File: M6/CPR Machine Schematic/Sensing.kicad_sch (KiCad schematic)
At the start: 9 parts, among them J12 I2C Port, J8 Force Sensor, U3 MCP6004, U5 MCP3021A0T-E_OT

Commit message: Final PCB
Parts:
- R16: value 80.6 Ohm -> 80.6 kOhm
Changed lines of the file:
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@@
 	(rectangle
 		(start 19.685 27.94)
-		(end 128.905 102.87)
+		(end 128.27 97.155)
 		(stroke
 			(width 0)
@@
 			)
 		)
-		(property "Value" "80.6 Ohm"
+		(property "Value" "80.6 kOhm"
 			(at 58.42 66.04 90)
 			(effects

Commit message: Board V2 Final
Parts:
- C13, C_OPT1, J8, R16, R17: now left out of the parts list
- U3, U5: Notes (none) -> Have: 1
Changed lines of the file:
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@@
 		(unit 1)
 		(exclude_from_sim no)
-		(in_bom yes)
+		(in_bom no)
 		(on_board yes)
 		(dnp yes)
@@
 		)
 		(property "digikey" "1292-1206N470J102CT-ND"
+			(at 74.93 54.61 0)
+			(effects
+				(font
+					(size 1.27 1.27)
+				)
+				(hide yes)
+			)
+		)
+		(property "Notes" ""
 			(at 74.93 54.61 0)
 			(effects
@@
 			)
 		)
+		(property "Notes" ""
+			(at 35.56 21.59 0)
+			(effects
+				(font
+					(size 1.27 1.27)
+				)
+				(hide yes)
+			)
+		)
 		(pin "2"
 		)
@@
 			)
 		)
+		(property "Notes" "Have: 1"
+			(at 102.87 48.26 0)
+			(effects
+				(font
+					(size 1.27 1.27)
+				)
+				(hide yes)
+			)
+		)
 		(pin "3"
 		)
@@
 		(unit 1)
 		(exclude_from_sim no)
-		(in_bom yes)
+		(in_bom no)
 		(on_board yes)
 		(dnp no)
@@
 			)
 		)
+		(property "Notes" ""
+			(at 40.64 86.36 0)
+			(effects
+				(font
+					(size 1.27 1.27)
+				)
+				(hide yes)
+			)
+		)
 		(pin "2"
 		)
@@
 		(unit 1)
 		(exclude_from_sim no)
-		(in_bom yes)
+		(in_bom no)
 		(on_board yes)
 		(dnp no)
@@
 			)
 		)
+		(property "Notes" ""
+			(at 58.42 80.01 90)
+			(effects
+				(font
+					(size 1.27 1.27)
+				)
+				(hide yes)
+			)
+		)
 		(pin "1"
 		)
@@
 		(unit 1)
 		(exclude_from_sim no)
-		(in_bom yes)
+		(in_bom no)
 		(on_board yes)
 		(dnp no)
@@
 			)
 		)
+		(property "Notes" ""
+			(at 58.42 69.85 90)
+			(effects
+				(font
+					(size 1.27 1.27)
+				)
+				(hide yes)
+			)
+		)
 		(pin "2"
 		)
@@
 			)
 		)
+		(property "Notes" "Have: 1"
+			(at 59.69 48.26 0)
+			(effects
+				(font
+					(size 1.27 1.27)
+				)
+				(hide yes)
+			)
+		)
 		(pin "4"
 		)
@@
 			)
 		)
+		(property "Notes" ""
+			(at 34.29 49.53 0)
+			(effects
+				(font
+					(size 1.27 1.27)
+				)
+				(hide yes)
+			)
+		)
 		(pin "2"
 		)
@@
 		(unit 1)
 		(exclude_from_sim no)
-		(in_bom yes)
+		(in_bom no)
 		(on_board yes)
 		(dnp no)
@@
 			(at 34.29 41.91 0)
 			(effects
+				(font
+					(size 1.27 1.27)
+				)
+				(hide yes)
+			)
+		)
+		(property "Notes" ""
+			(at 34.29 41.91 0)
+			(effects

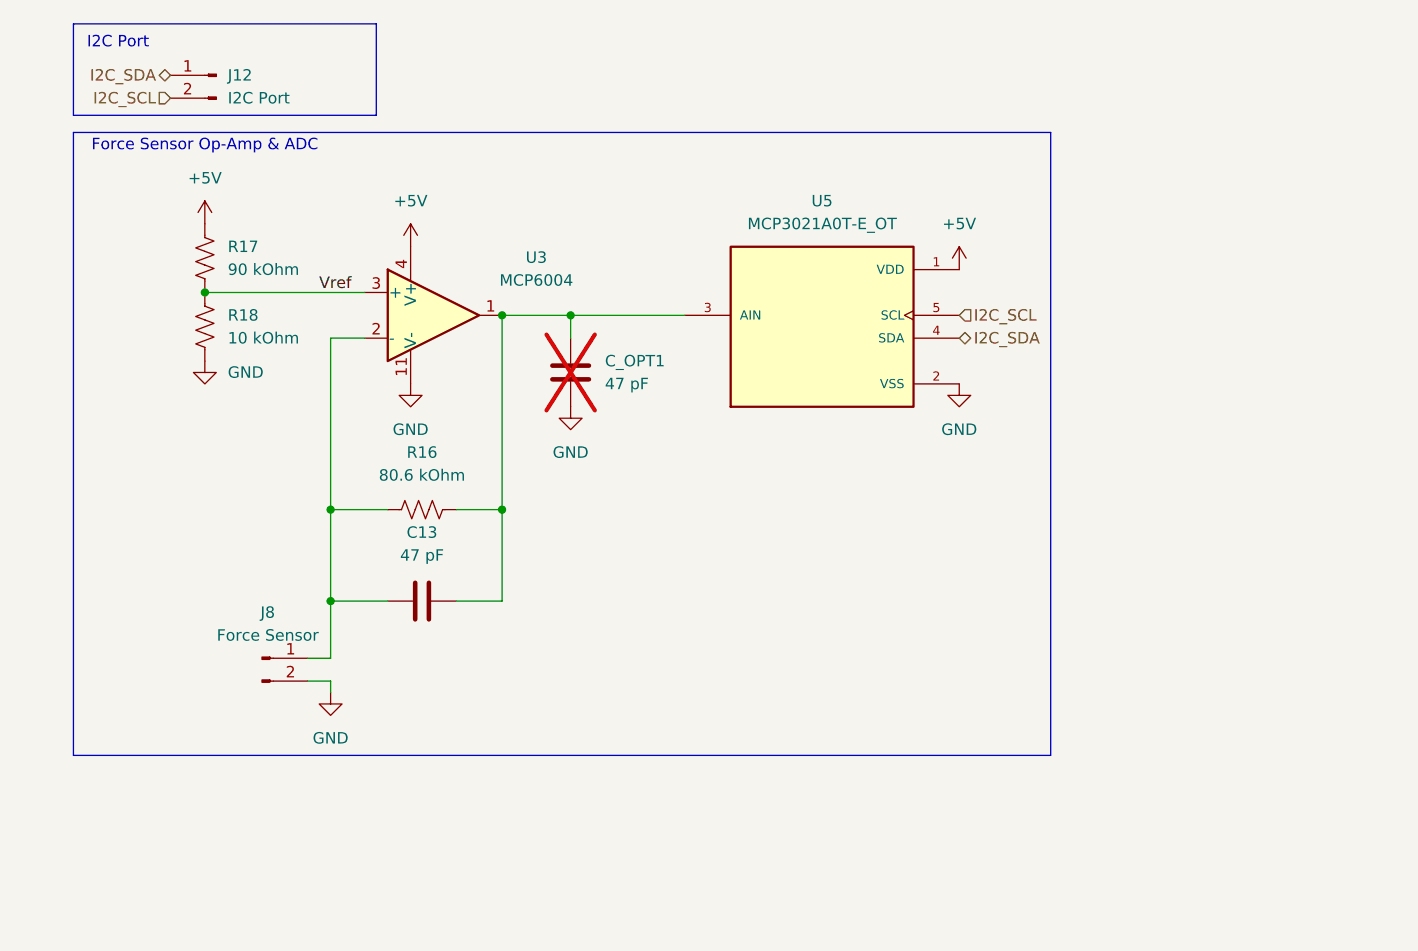
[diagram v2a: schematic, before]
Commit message: Voltage readout, MUX, Debouncing Caps
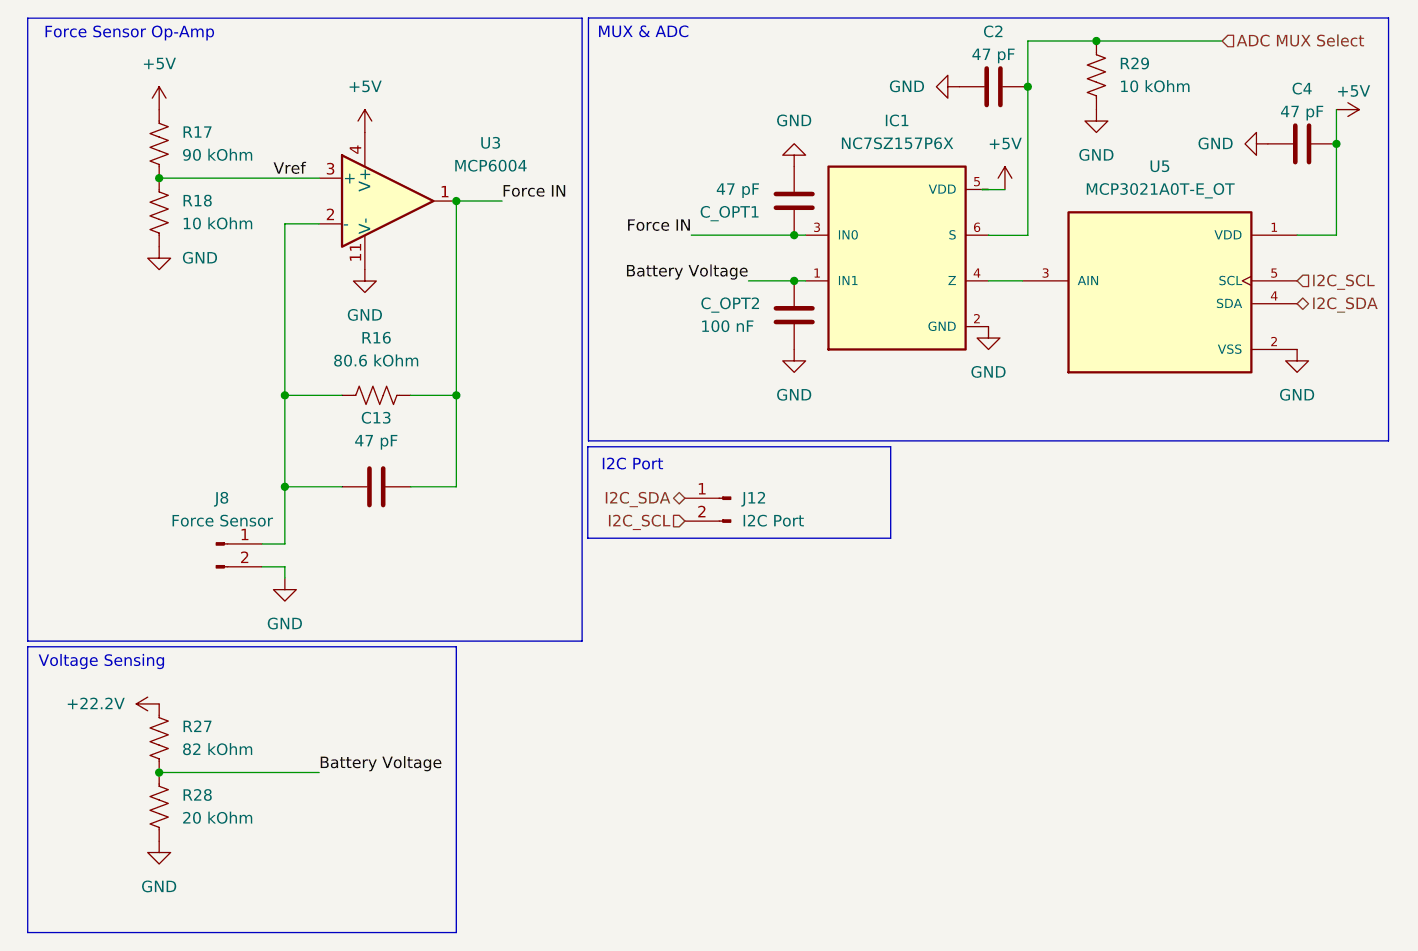
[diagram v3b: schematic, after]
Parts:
- added C2, C4: 47 pF, Capacitor_SMD:C_1206_3216Metric_Pad1.33x1.80mm_HandSolder, symbol Device:C
- added C_OPT2: 100 nF, Capacitor_SMD:C_1206_3216Metric_Pad1.33x1.80mm_HandSolder, symbol Device:C
- added IC1: NC7SZ157P6X, NC7SZ157P6X:SC70-6L, symbol NC7SZ157P6X:NC7SZ157P6X
- added R27: 82 kOhm, symbol Device:R_US
- added R28: 20 kOhm, symbol Device:R_US
- added R29: 10 kOhm, Resistor_SMD:R_1206_3216Metric_Pad1.30x1.75mm_HandSolder, symbol Device:R_US
- C_OPT1: now fitted; now in the parts list
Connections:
- net +5V: now also C4.2, IC1.5 (VDD)
- net GND: now also C2.1, C4.1, C_OPT2.1, IC1.2 (GND), R28.2, R29.2
- net Force IN: now reaches C13.2, C_OPT1.2, R16.1, U3.1
- net Force IN: now also IC1.3 (IN0); no longer U5.3 (AIN)
- new net: IC1.4 (Z), U5.3 (AIN)
- new net +22.2V: R27.1
- new net ADC MUX Select: C2.2, IC1.6 (S), R29.1
- new net Battery Voltage: C_OPT2.2, IC1.1 (IN1), R27.2, R28.1
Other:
- note added: "Force Sensor Op-Amp"
- note added: "MUX & ADC"
- note added: "Voltage Sensing"
- note removed: "Force Sensor Op-Amp & ADC"
- moved on the sheet: C13, J12, J8, R16, R17, R18, U3, U5

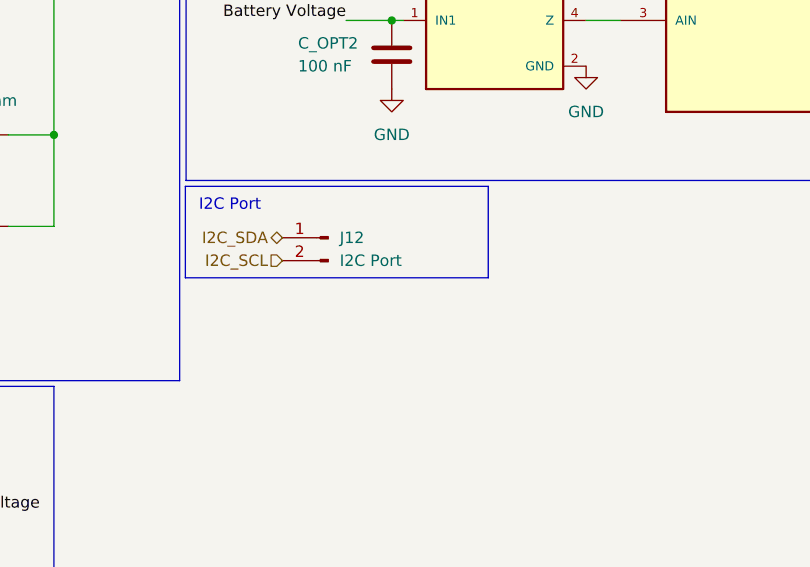
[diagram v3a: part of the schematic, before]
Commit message: MUX, Debounce Caps, I2C Testpoints
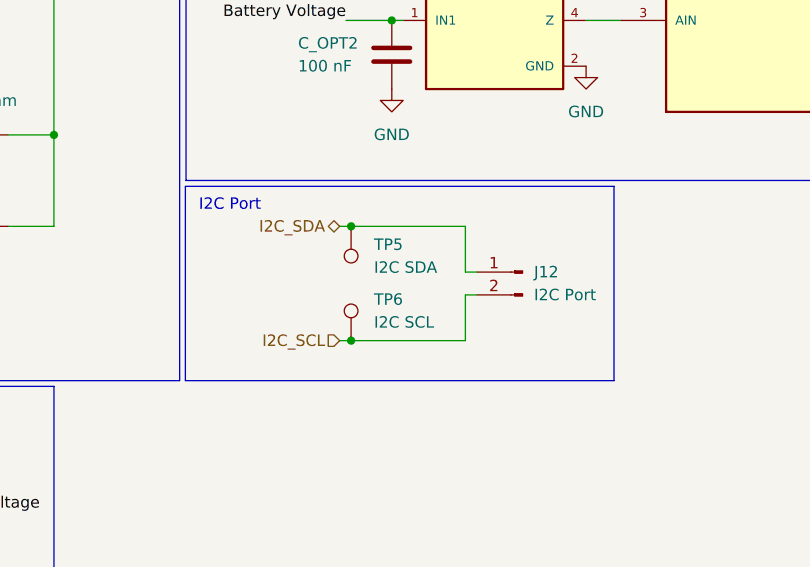
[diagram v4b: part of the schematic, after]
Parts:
- added TP5: I2C SDA, TestPoint:TestPoint_Pad_D3.0mm, symbol Connector:TestPoint
- added TP6: I2C SCL, TestPoint:TestPoint_Pad_D3.0mm, symbol Connector:TestPoint
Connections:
- net I2C_SCL: now also TP6.1
- net I2C_SDA: now also TP5.1
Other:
- moved on the sheet: J12
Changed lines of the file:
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@@
 	(rectangle
 		(start 76.835 62.865)
-		(end 110.49 73.025)
+		(end 124.46 84.455)
 		(stroke
 			(width 0)
@@
 	)
 	(junction
+		(at 95.25 67.31)
+		(diameter 0)
+		(color 0 0 0 0)
+	)
+	(junction
 		(at 43.18 67.31)
 		(diameter 0)
@@
 		(color 0 0 0 0)
 	)
+	(junction
+		(at 95.25 80.01)
+		(diameter 0)
+		(color 0 0 0 0)
+	)
 	(wire
 		(pts
@@
 	(wire
 		(pts
+			(xy 95.25 80.01) (xy 93.98 80.01)
+		)
+		(stroke
+			(width 0)
+			(type default)
+		)
+	)
+	(wire
+		(pts
 			(xy 99.7691 39.3524) (xy 101.0391 39.3524)
 		)
@@
 	(wire
 		(pts
+			(xy 107.95 80.01) (xy 95.25 80.01)
+		)
+		(stroke
+			(width 0)
+			(type default)
+		)
+	)
+	(wire
+		(pts
 			(xy 57.15 67.31) (xy 62.23 67.31)
 		)
@@
 	(wire
 		(pts
+			(xy 107.95 72.39) (xy 109.22 72.39)
+		)
+		(stroke
+			(width 0)
+			(type default)
+		)
+	)
+	(wire
+		(pts
 			(xy 133.35 17.78) (xy 147.32 17.78)
 		)
@@
 	(wire
 		(pts
+			(xy 107.95 67.31) (xy 107.95 72.39)
+		)
+		(stroke
+			(width 0)
+			(type default)
+		)
+	)
+	(wire
+		(pts
 			(xy 29.21 33.02) (xy 46.99 33.02)
 		)
@@
 	(wire
 		(pts
+			(xy 95.25 67.31) (xy 107.95 67.31)
+		)
+		(stroke
+			(width 0)
+			(type default)
+		)
+	)
+	(wire
+		(pts
 			(xy 62.23 57.15) (xy 62.23 35.56)
 		)
@@
 	(wire
 		(pts
+			(xy 93.98 67.31) (xy 95.25 67.31)
+		)
+		(stroke
+			(width 0)
+			(type default)
+		)
+	)
+	(wire
+		(pts
 			(xy 62.23 35.56) (xy 67.31 35.56)
 		)
@@
 	(wire
 		(pts
+			(xy 107.95 74.93) (xy 107.95 80.01)
+		)
+		(stroke
+			(width 0)
+			(type default)
+		)
+	)
+	(wire
+		(pts
 			(xy 29.21 99.06) (xy 46.99 99.06)
 		)
@@
 		(pts
 			(xy 125.73 17.78) (xy 125.73 22.86)
+		)
+		(stroke
+			(width 0)
+			(type default)
+		)
+	)
+	(wire
+		(pts
+			(xy 107.95 74.93) (xy 109.22 74.93)
 		)
 		(stroke
@@
 	(hierarchical_label "I2C_SCL"
 		(shape input)
-		(at 87.63 71.12 180)
+		(at 93.98 80.01 180)
 		(effects
 			(font
@@
 	(hierarchical_label "I2C_SDA"
 		(shape bidirectional)
-		(at 87.63 68.58 180)
+		(at 93.98 67.31 180)
 		(effects
 			(font
@@
 	(symbol
 		(lib_id "Connector:Conn_01x02_Pin")
-		(at 92.71 68.58 0)
+		(at 114.3 72.39 0)
 		(mirror y)
 		(unit 1)
@@
 		(fields_autoplaced yes)
 		(property "Reference" "J12"
-			(at 93.98 68.5799 0)
+			(at 115.57 72.3899 0)
 			(effects
 				(font
@@
 		)
 		(property "Value" "I2C Port"
-			(at 93.98 71.1199 0)
+			(at 115.57 74.9299 0)
 			(effects
 				(font
@@
 		)
 		(property "Footprint" "Connector_PinHeader_2.54mm:PinHeader_1x02_P2.54mm_Vertical"
-			(at 92.71 68.58 0)
+			(at 114.3 72.39 0)
 			(effects
 				(font
@@
 		)
 		(property "Datasheet" "~"
-			(at 92.71 68.58 0)
+			(at 114.3 72.39 0)
 			(effects
 				(font
@@
 		)
 		(property "Description" "Generic connector, single row, 01x02, script generated"
-			(at 92.71 68.58 0)
+			(at 114.3 72.39 0)
 			(effects
 				(font
@@
 		)
 		(property "Notes" ""
-			(at 92.71 68.58 0)
+			(at 114.3 72.39 0)
 			(effects
 				(font
@@
 	)
 	(symbol
+		(lib_id "Connector:TestPoint")
+		(at 95.25 80.01 0)
+		(unit 1)
+		(exclude_from_sim no)
+		(in_bom yes)
+		(on_board yes)
+		(dnp no)
+		(fields_autoplaced yes)
+		(property "Reference" "TP6"
+			(at 97.79 75.4379 0)
+			(effects
+				(font
+					(size 1.27 1.27)
+				)
+				(justify left)
+			)
+		)
+		(property "Value" "I2C SCL"
+			(at 97.79 77.9779 0)
+			(effects
+				(font
+					(size 1.27 1.27)
+				)
+				(justify left)
+			)
+		)
+		(property "Footprint" "TestPoint:TestPoint_Pad_D3.0mm"
+			(at 100.33 80.01 0)
+			(effects
+				(font
+					(size 1.27 1.27)
+				)
+				(hide yes)
+			)
+		)
+		(property "Datasheet" "~"
+			(at 100.33 80.01 0)
+			(effects
+				(font
+					(size 1.27 1.27)
+				)
+				(hide yes)
+			)
+		)
+		(property "Description" "test point"
+			(at 95.25 80.01 0)
+			(effects
+				(font
+					(size 1.27 1.27)
+				)
+				(hide yes)
+			)
+		)
+		(pin "1"
+		)
+		(instances
+			(project "CPR Machine Schematic"
+				(path "/8991fc77-975f-4978-a089-6b2a5e33f59b/2e704a40-db78-4cf7-9f7e-cfc586f5aeb3"
+					(reference "TP6")
+					(unit 1)
+				)
+			)
+		)
+	)
+	(symbol
 		(lib_id "power:GND")
 		(at 118.11 22.86 270)
@@
 					(unit 1)
 				)
+			)
+		)
+	)
+	(symbol
+		(lib_id "Connector:TestPoint")
+		(at 95.25 67.31 180)
+		(unit 1)
+		(exclude_from_sim no)
+		(in_bom yes)
+		(on_board yes)
+		(dnp no)
+		(fields_autoplaced yes)
+		(property "Reference" "TP5"
+			(at 97.79 69.3419 0)
+			(effects
+				(font
+					(size 1.27 1.27)
+				)
+				(justify right)
+			)
+		)
+		(property "Value" "I2C SDA"
+			(at 97.79 71.8819 0)
+			(effects
+				(font
+					(size 1.27 1.27)
+				)
+				(justify right)
+			)
+		)
+		(property "Footprint" "TestPoint:TestPoint_Pad_D3.0mm"
+			(at 90.17 67.31 0)
+			(effects
+				(font
+					(size 1.27 1.27)
+				)
+				(hide yes)
+			)
+		)
+		(property "Datasheet" "~"
+			(at 90.17 67.31 0)
+			(effects
+				(font
+					(size 1.27 1.27)
+				)
+				(hide yes)
+			)
+		)
+		(property "Description" "test point"
+			(at 95.25 67.31 0)
+			(effects
+				(font
+					(size 1.27 1.27)
+				)
+				(hide yes)
+			)
+		)
+		(pin "1"
+		)
+		(instances
+			(project ""
+				(path "/8991fc77-975f-4978-a089-6b2a5e33f59b/2e704a40-db78-4cf7-9f7e-cfc586f5aeb3"
+					(reference "TP5")
+					(unit 1)
+				)
